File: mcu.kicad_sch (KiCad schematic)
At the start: 0 parts

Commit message: Working on power board
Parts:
- added C19: 100nF, Capacitor_SMD:C_1206_3216Metric, symbol Device:C
- added U4: ADAFRUIT_QT_PY, ADAFRUIT_QT_PY:MODULE_ADAFRUIT_QT_PY, symbol _RP2040:ADAFRUIT_QT_PY
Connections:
- new net +3V3: U4.12 (3V3)
- new net +5V: C19.1, U4.14 (5V)
- new net BOOST_A_PWR_EN: U4.2 (A1/D1)
- new net BOOST_A_PWR_GOOD: U4.1 (A0/D0/DAC)
- new net BOOST_B_PWR_EN: U4.4 (A3/D3)
- new net BOOST_B_PWR_GOOD: U4.3 (A2/D2)
- new net GND: C19.2, U4.13 (GND)
- no-connect marks 0 -> 5
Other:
- note added: "CHECK INPUT FILTER!!"

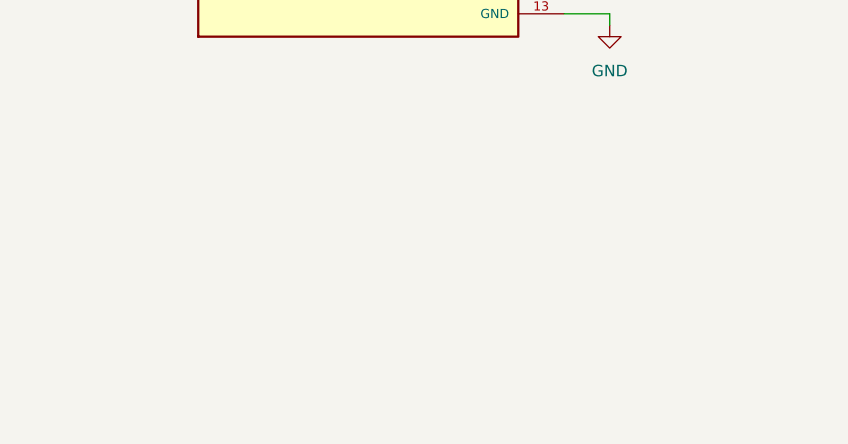
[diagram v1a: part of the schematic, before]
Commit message: Working on load switch design
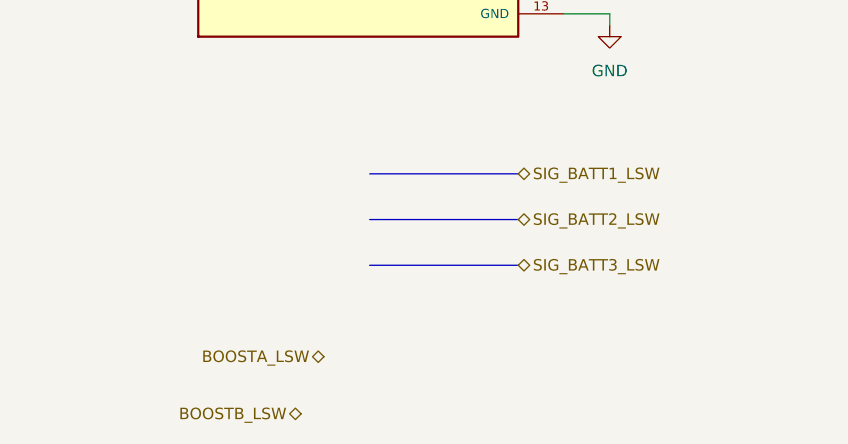
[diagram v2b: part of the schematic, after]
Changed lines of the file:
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@@
+	(bus
+		(pts
+			(xy 147.32 130.81) (xy 163.83 130.81)
+		)
+		(stroke
+			(width 0)
+			(type default)
+		)
+	)
 	(bus
 		(pts
@@
 	(bus
 		(pts
+			(xy 147.32 140.97) (xy 163.83 140.97)
+		)
+		(stroke
+			(width 0)
+			(type default)
+		)
+	)
+	(bus
+		(pts
 			(xy 97.79 107.95) (xy 97.79 110.49)
+		)
+		(stroke
+			(width 0)
+			(type default)
+		)
+	)
+	(bus
+		(pts
+			(xy 147.32 135.89) (xy 163.83 135.89)
 		)
 		(stroke
@@
 		)
 	)
+	(hierarchical_label "SIG_BATT2_LSW"
+		(shape bidirectional)
+		(at 163.83 135.89 0)
+		(effects
+			(font
+				(size 1.27 1.27)
+			)
+			(justify left)
+		)
+	)
+	(hierarchical_label "SIG_BATT3_LSW"
+		(shape bidirectional)
+		(at 163.83 140.97 0)
+		(effects
+			(font
+				(size 1.27 1.27)
+			)
+			(justify left)
+		)
+	)
+	(hierarchical_label "BOOSTA_LSW"
+		(shape bidirectional)
+		(at 142.24 151.13 180)
+		(effects
+			(font
+				(size 1.27 1.27)
+			)
+			(justify right)
+		)
+	)
 	(hierarchical_label "BOOST_A_SIG"
 		(shape bidirectional)
@@
 		)
 	)
+	(hierarchical_label "BOOSTB_LSW"
+		(shape bidirectional)
+		(at 139.7 157.48 180)
+		(effects
+			(font
+				(size 1.27 1.27)
+			)
+			(justify right)
+		)
+	)
+	(hierarchical_label "SIG_BATT1_LSW"
+		(shape bidirectional)
+		(at 163.83 130.81 0)
+		(effects
+			(font
+				(size 1.27 1.27)
+			)
+			(justify left)
+		)
+	)

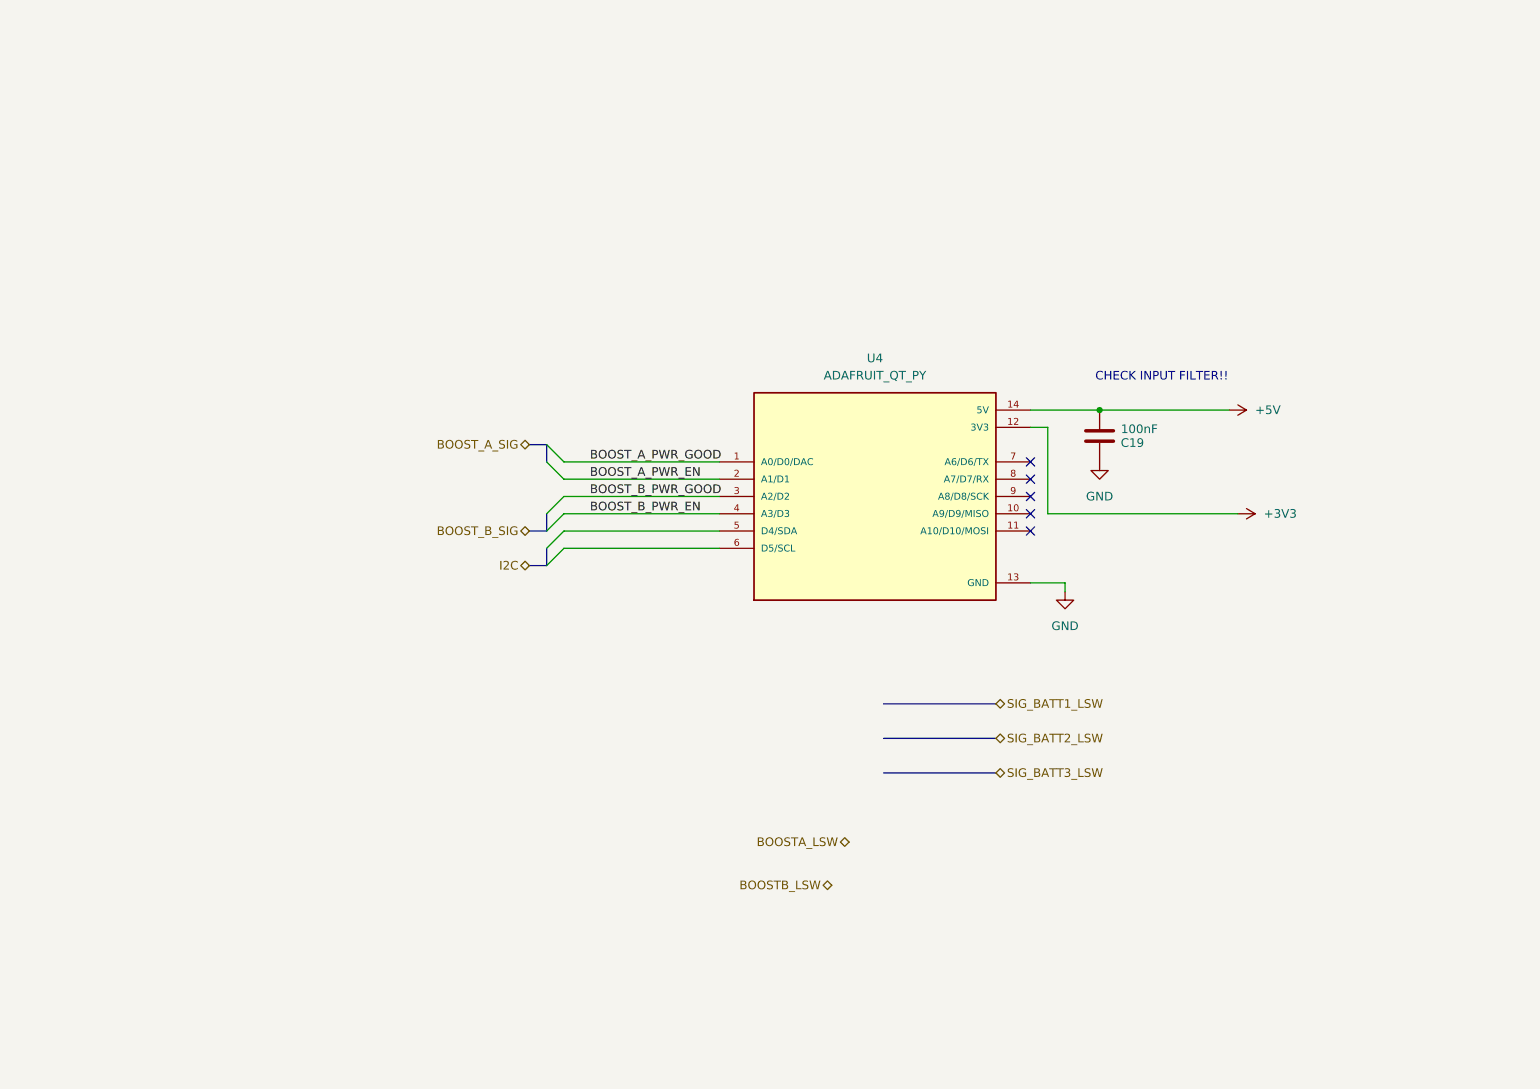
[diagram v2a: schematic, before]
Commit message: Adding in connections to schematic
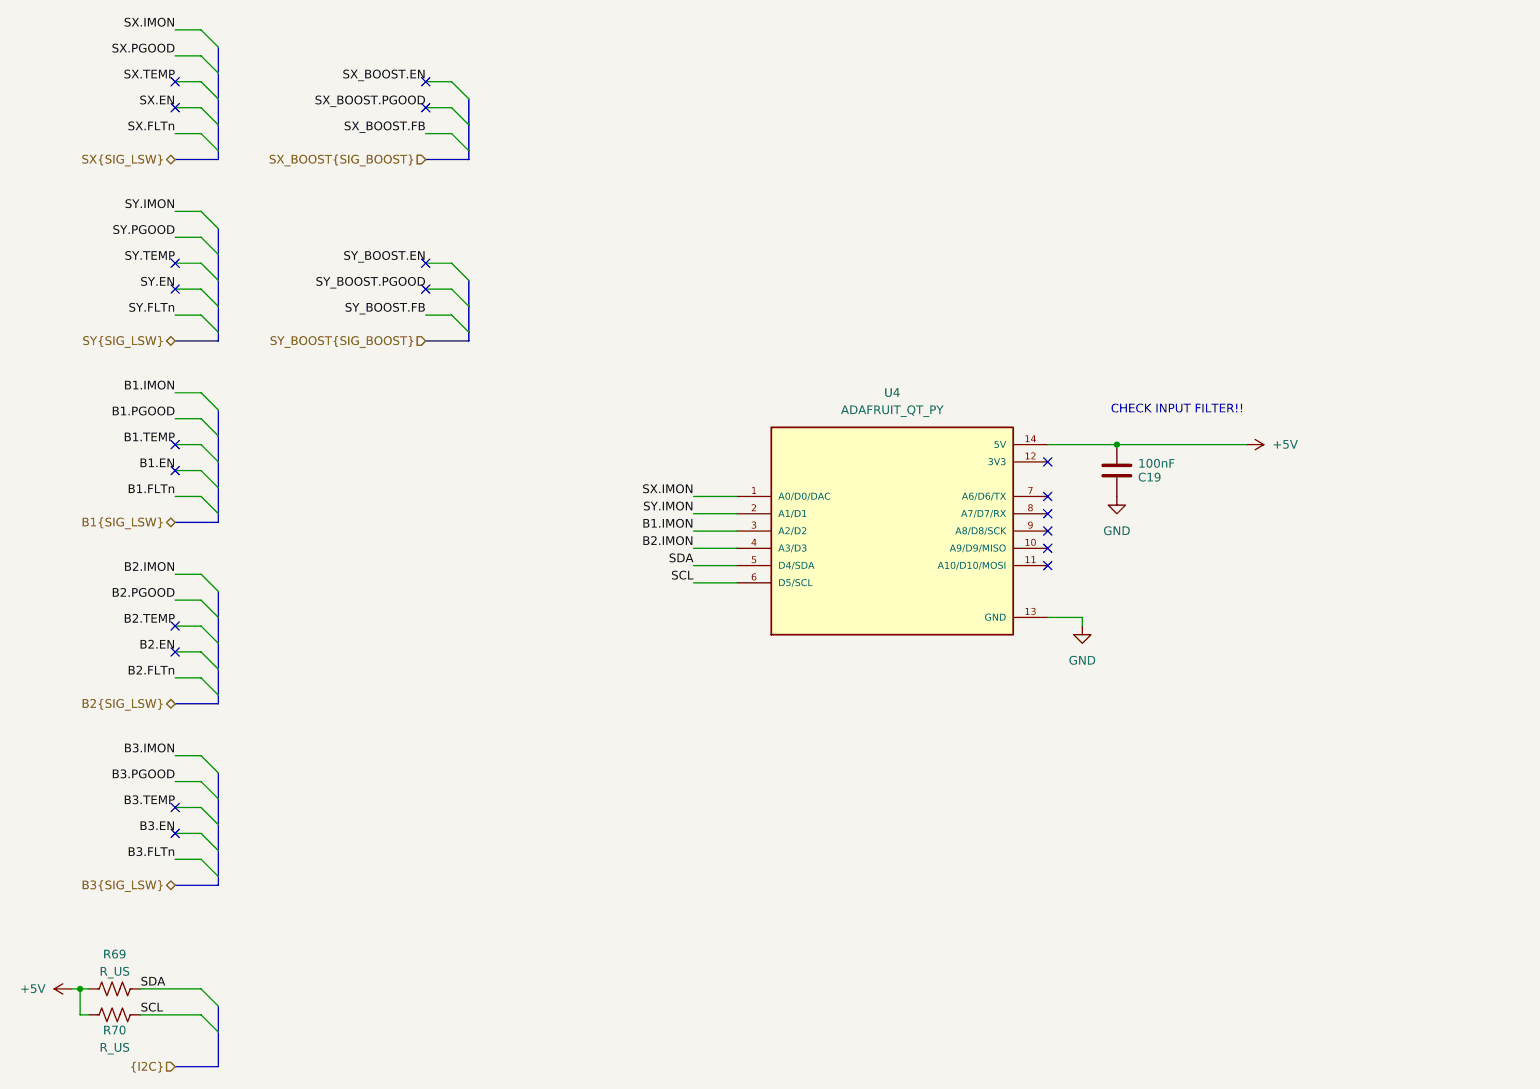
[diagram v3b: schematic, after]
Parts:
- added R69, R70: R_US, symbol Device:R_US
- U4: footprint ADAFRUIT_QT_PY:MODULE_ADAFRUIT_QT_PY -> _Power_Board:MODULE_ADAFRUIT_QT_PY
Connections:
- net +5V: now also R69.1, R70.2
- net SDA: now reaches U4.5 (D4/SDA)
- net SDA: now also R69.2
- net SCL: now reaches U4.6 (D5/SCL)
- net SCL: now also R70.1
- net +3V3: no longer names the net of U4.12 (3V3)
- net BOOST_A_PWR_EN renamed SY.IMON
- net BOOST_A_PWR_GOOD renamed SX.IMON
- net BOOST_B_PWR_EN renamed B2.IMON
- net BOOST_B_PWR_GOOD renamed B1.IMON
- no-connect marks 5 -> 20
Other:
- company: (none) -> Solar Airplane
- title: (none) -> House keeping
- moved on the sheet: C19, U4

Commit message: Working on layout now
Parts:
- removed R69, R70: R_US, symbol Device:R_US
- added R6, R7: 33k, Resistor_SMD:R_0603_1608Metric, symbol Device:R_US
- renumbered U4 to U3
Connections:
- net +5V: now also R6.1, R7.2
- net SCL: now also R7.1
- net SDA: now also R6.2

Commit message: Working on layout for dev board
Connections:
- net SX.EN: now also U3.9 (A8/D8/SCK)
- net SX_BOOST.EN: now also U3.7 (A6/D6/TX)
- net SY.EN: now also U3.10 (A9/D9/MISO)
- net SY_BOOST.EN: now also U3.8 (A7/D7/RX)
- no-connect marks 20 -> 16
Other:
- moved on the sheet: C19
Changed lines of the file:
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@@
 	)
 	(junction
-		(at 181.61 92.71)
+		(at 198.12 92.71)
 		(diameter 0)
 		(color 0 0 0 0)
@@
 	)
 	(no_connect
-		(at 171.45 107.95)
-	)
-	(no_connect
 		(at 171.45 95.25)
-	)
-	(no_connect
-		(at 171.45 102.87)
 	)
 	(no_connect
@@
 	)
 	(no_connect
-		(at 171.45 100.33)
-	)
-	(no_connect
 		(at 43.18 39.37)
 	)
@@
 		(at 80.01 39.37)
 	)
-	(no_connect
-		(at 171.45 105.41)
-	)
 	(bus_entry
 		(at 86.36 72.39)
@@
 	(wire
 		(pts
+			(xy 171.45 107.95) (xy 177.8 107.95)
+		)
+		(stroke
+			(width 0)
+			(type default)
+		)
+	)
+	(wire
+		(pts
 			(xy 46.99 66.04) (xy 43.18 66.04)
 		)
@@
 		)
 	)
+	(wire
+		(pts
+			(xy 177.8 102.87) (xy 171.45 102.87)
+		)
+		(stroke
+			(width 0)
+			(type default)
+		)
+	)
 	(bus
 		(pts
@@
 	(wire
 		(pts
+			(xy 177.8 100.33) (xy 171.45 100.33)
+		)
+		(stroke
+			(width 0)
+			(type default)
+		)
+	)
+	(wire
+		(pts
 			(xy 46.99 142.24) (xy 43.18 142.24)
 		)
@@
 	(wire
 		(pts
+			(xy 171.45 105.41) (xy 177.8 105.41)
+		)
+		(stroke
+			(width 0)
+			(type default)
+		)
+	)
+	(wire
+		(pts
 			(xy 46.99 96.52) (xy 43.18 96.52)
 		)
@@
 	(wire
 		(pts
-			(xy 171.45 92.71) (xy 181.61 92.71)
+			(xy 171.45 92.71) (xy 198.12 92.71)
 		)
 		(stroke
@@
 	(wire
 		(pts
+			(xy 198.12 92.71) (xy 209.55 92.71)
+		)
+		(stroke
+			(width 0)
+			(type default)
+		)
+	)
+	(wire
+		(pts
 			(xy 119.38 110.49) (xy 125.73 110.49)
 		)
@@
 		(pts
 			(xy 80.01 50.8) (xy 86.36 50.8)
-		)
-		(stroke
-			(width 0)
-			(type default)
-		)
-	)
-	(wire
-		(pts
-			(xy 181.61 92.71) (xy 200.66 92.71)
 		)
 		(stroke
@@
 		)
 	)
+	(label "SY_BOOST.EN"
+		(at 177.8 102.87 0)
+		(effects
+			(font
+				(size 1.27 1.27)
+			)
+			(justify left bottom)
+		)
+	)
 	(label "SX.FLTn"
 		(at 43.18 46.99 180)
@@
 		)
 	)
+	(label "SY.EN"
+		(at 177.8 107.95 0)
+		(effects
+			(font
+				(size 1.27 1.27)
+			)
+			(justify left bottom)
+		)
+	)
 	(label "SDA"
 		(at 38.1 172.72 0)
@@
 		)
 	)
+	(label "SX.EN"
+		(at 177.8 105.41 0)
+		(effects
+			(font
+				(size 1.27 1.27)
+			)
+			(justify left bottom)
+		)
+	)
 	(label "SY_BOOST.EN"
 		(at 80.01 66.04 180)
@@
 			)
 			(justify right bottom)
+		)
+	)
+	(label "SX_BOOST.EN"
+		(at 177.8 100.33 0)
+		(effects
+			(font
+				(size 1.27 1.27)
+			)
+			(justify left bottom)
 		)
 	)
@@
 	(symbol
 		(lib_id "Device:C")
-		(at 181.61 96.52 0)
+		(at 198.12 96.52 0)
 		(unit 1)
 		(exclude_from_sim no)
@@
 		(dnp no)
 		(property "Reference" "C19"
-			(at 186.436 97.536 0)
+			(at 202.946 97.536 0)
 			(effects
 				(font
@@
 		)
 		(property "Value" "100nF"
-			(at 187.452 95.504 0)
+			(at 203.962 95.504 0)
 			(effects
 				(font
@@
 		)
 		(property "Footprint" "Capacitor_SMD:C_1206_3216Metric"
-			(at 182.5752 100.33 0)
+			(at 199.0852 100.33 0)
 			(effects
 				(font
@@
 		)
 		(property "Datasheet" "https://search.murata.co.jp/Ceramy/image/img/A01X/G101/ENG/GCM31C5C1H104FA16-01.pdf"
-			(at 181.61 96.52 0)
+			(at 198.12 96.52 0)
 			(effects
 				(font
@@
 		)
 		(property "Description" "CAP CER 0.1UF 50V C0G/NP0 1206"
-			(at 181.61 96.52 0)
+			(at 198.12 96.52 0)
 			(effects
 				(font
@@
 		)
 		(property "Mfr" "Murata Electronics"
-			(at 181.61 96.52 0)
+			(at 198.12 96.52 0)
 			(effects
 				(font
@@
 		)
 		(property "Mfr P/N" "GCM31C5C1H104FA16L"
-			(at 181.61 96.52 0)
+			(at 198.12 96.52 0)
 			(effects
 				(font
@@
 		)
 		(property "Supplier_1" "Digikey"
-			(at 181.61 96.52 0)
+			(at 198.12 96.52 0)
 			(effects
 				(font
@@
 		)
 		(property "Supplier_1 P/N" "490-GCM31C5C1H104FA16LTR-ND"
-			(at 181.61 96.52 0)
+			(at 198.12 96.52 0)
 			(effects
 				(font
@@
 		)
 		(property "Supplier_1 Unit Price" "0.98000"
-			(at 181.61 96.52 0)
+			(at 198.12 96.52 0)
 			(effects
 				(font
@@
 		)
 		(property "Supplier_1 Price @ Qty" "1"
-			(at 181.61 96.52 0)
+			(at 198.12 96.52 0)
 			(effects
 				(font
@@
 		)
 		(property "Supplier_2" ""
-			(at 181.61 96.52 0)
+			(at 198.12 96.52 0)
 			(effects
 				(font
@@
 		)
 		(property "Supplier_2 P/N" ""
-			(at 181.61 96.52 0)
+			(at 198.12 96.52 0)
 			(effects
 				(font
@@
 		)
 		(property "Supplier_2 Unit Price" ""
-			(at 181.61 96.52 0)
+			(at 198.12 96.52 0)
 			(effects
 				(font
@@
 		)
 		(property "Supplier_2 Price @ Qty" ""
-			(at 181.61 96.52 0)
+			(at 198.12 96.52 0)
 			(effects
 				(font
@@
 	(symbol
 		(lib_id "power:+5V")
-		(at 200.66 92.71 270)
+		(at 209.55 92.71 270)
 		(unit 1)
 		(exclude_from_sim no)
@@
 		(fields_autoplaced yes)
 		(property "Reference" "#PWR024"
-			(at 196.85 92.71 0)
+			(at 205.74 92.71 0)
 			(effects
 				(font
@@
 		)
 		(property "Value" "+5V"
-			(at 204.47 92.7099 90)
+			(at 213.36 92.7099 90)
 			(effects
 				(font
@@
 		)
 		(property "Footprint" ""
-			(at 200.66 92.71 0)
+			(at 209.55 92.71 0)
 			(effects
 				(font
@@
 		)
 		(property "Datasheet" ""
-			(at 200.66 92.71 0)
+			(at 209.55 92.71 0)
 			(effects
 				(font
@@
 		)
 		(property "Description" "Power symbol creates a global label with name \"+5V\""
-			(at 200.66 92.71 0)
+			(at 209.55 92.71 0)
 			(effects
 				(font
@@
 	(symbol
 		(lib_id "power:GND")
-		(at 181.61 100.33 0)
+		(at 198.12 100.33 0)
 		(unit 1)
 		(exclude_from_sim no)
@@
 		(fields_autoplaced yes)
 		(property "Reference" "#PWR023"
-			(at 181.61 106.68 0)
+			(at 198.12 106.68 0)
 			(effects
 				(font
@@
 		)
 		(property "Value" "GND"
-			(at 181.61 105.41 0)
+			(at 198.12 105.41 0)
 			(effects
 				(font
@@
 		)
 		(property "Footprint" ""
-			(at 181.61 100.33 0)
+			(at 198.12 100.33 0)
 			(effects
 				(font
@@
 		)
 		(property "Datasheet" ""
-			(at 181.61 100.33 0)
+			(at 198.12 100.33 0)
 			(effects
 				(font
@@
 		)
 		(property "Description" "Power symbol creates a global label with name \"GND\" , ground"
-			(at 181.61 100.33 0)
-			(effects
-				(font
+			(at 198.12 100.33 0)
+			(effects
+				(font

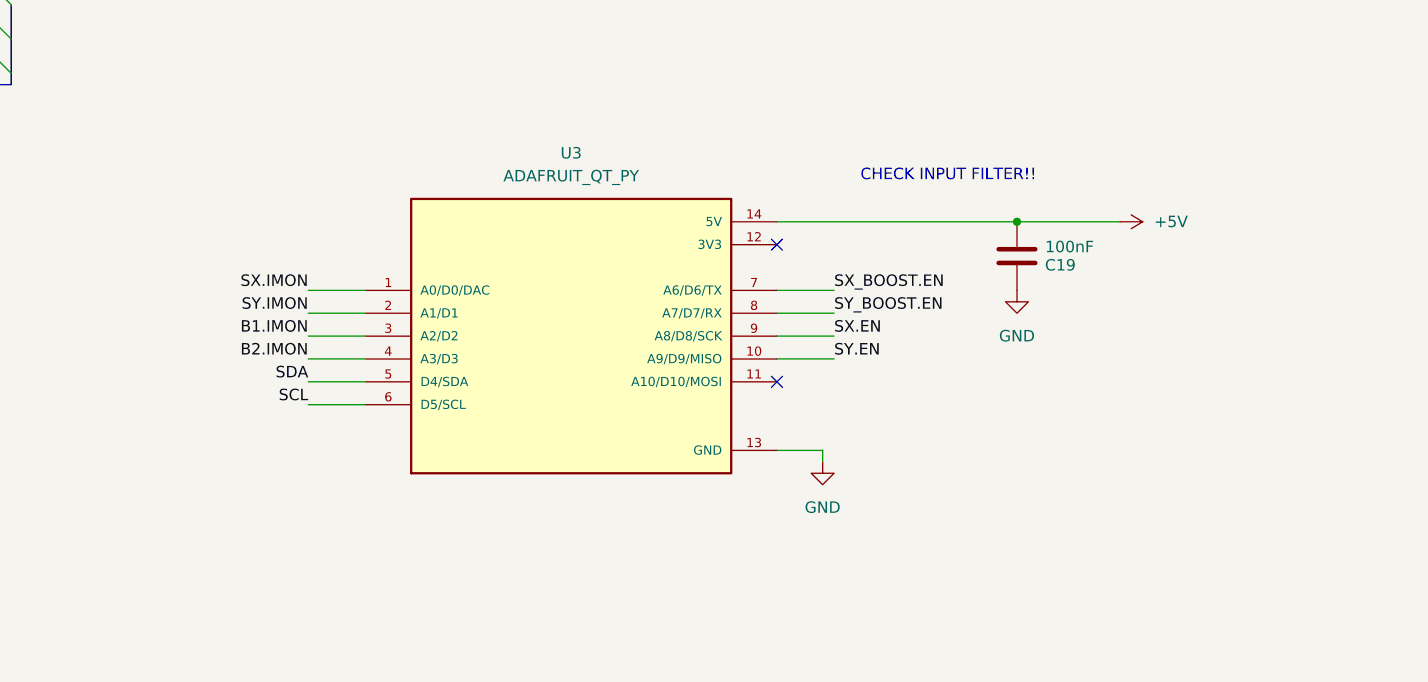
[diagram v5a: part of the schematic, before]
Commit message: Working on layout. Adding in TPs to schematic
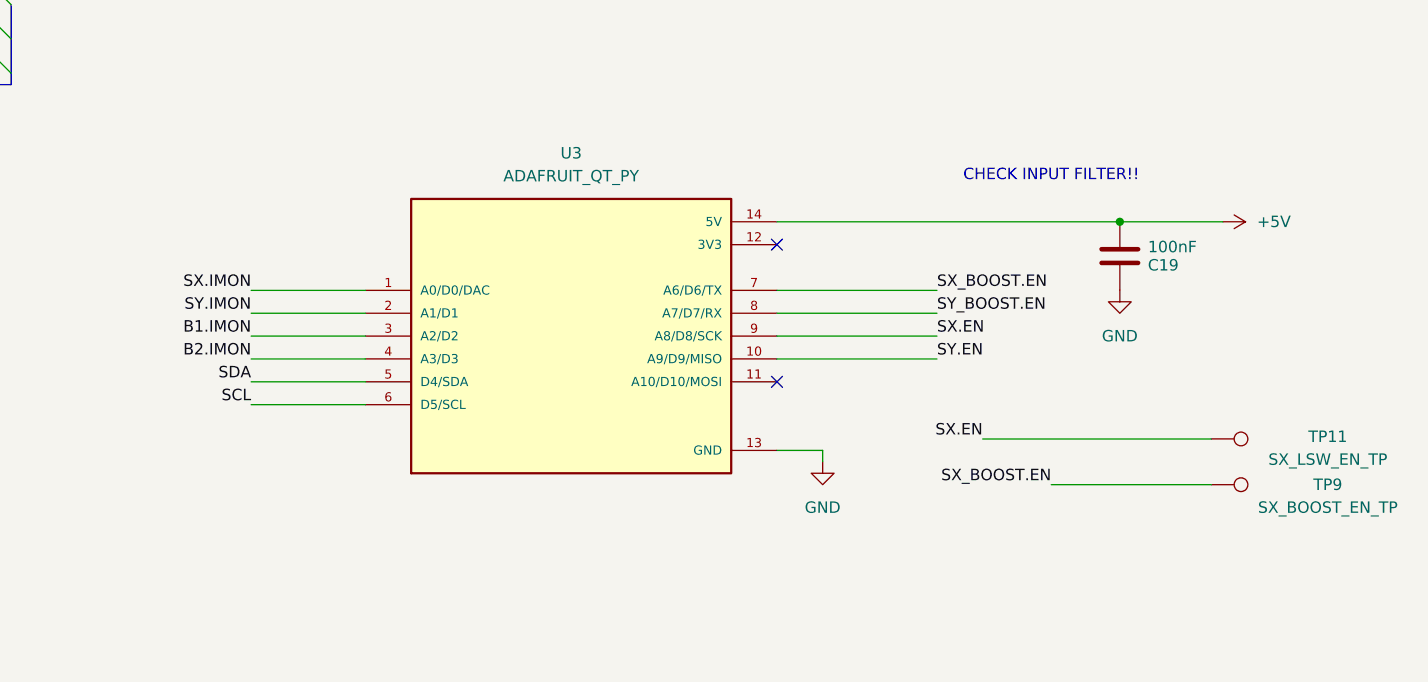
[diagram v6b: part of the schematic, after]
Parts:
- added TP11: SX_LSW_EN_TP, symbol Connector:TestPoint
- added TP9: SX_BOOST_EN_TP, symbol Connector:TestPoint
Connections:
- net SX.EN: now also TP11.1
- net SX_BOOST.EN: now also TP9.1
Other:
- moved on the sheet: C19
